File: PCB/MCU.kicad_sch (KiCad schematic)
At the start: 39 parts, among them J1 MSD-1-A, SW33V1 Conn_01x01_Pin

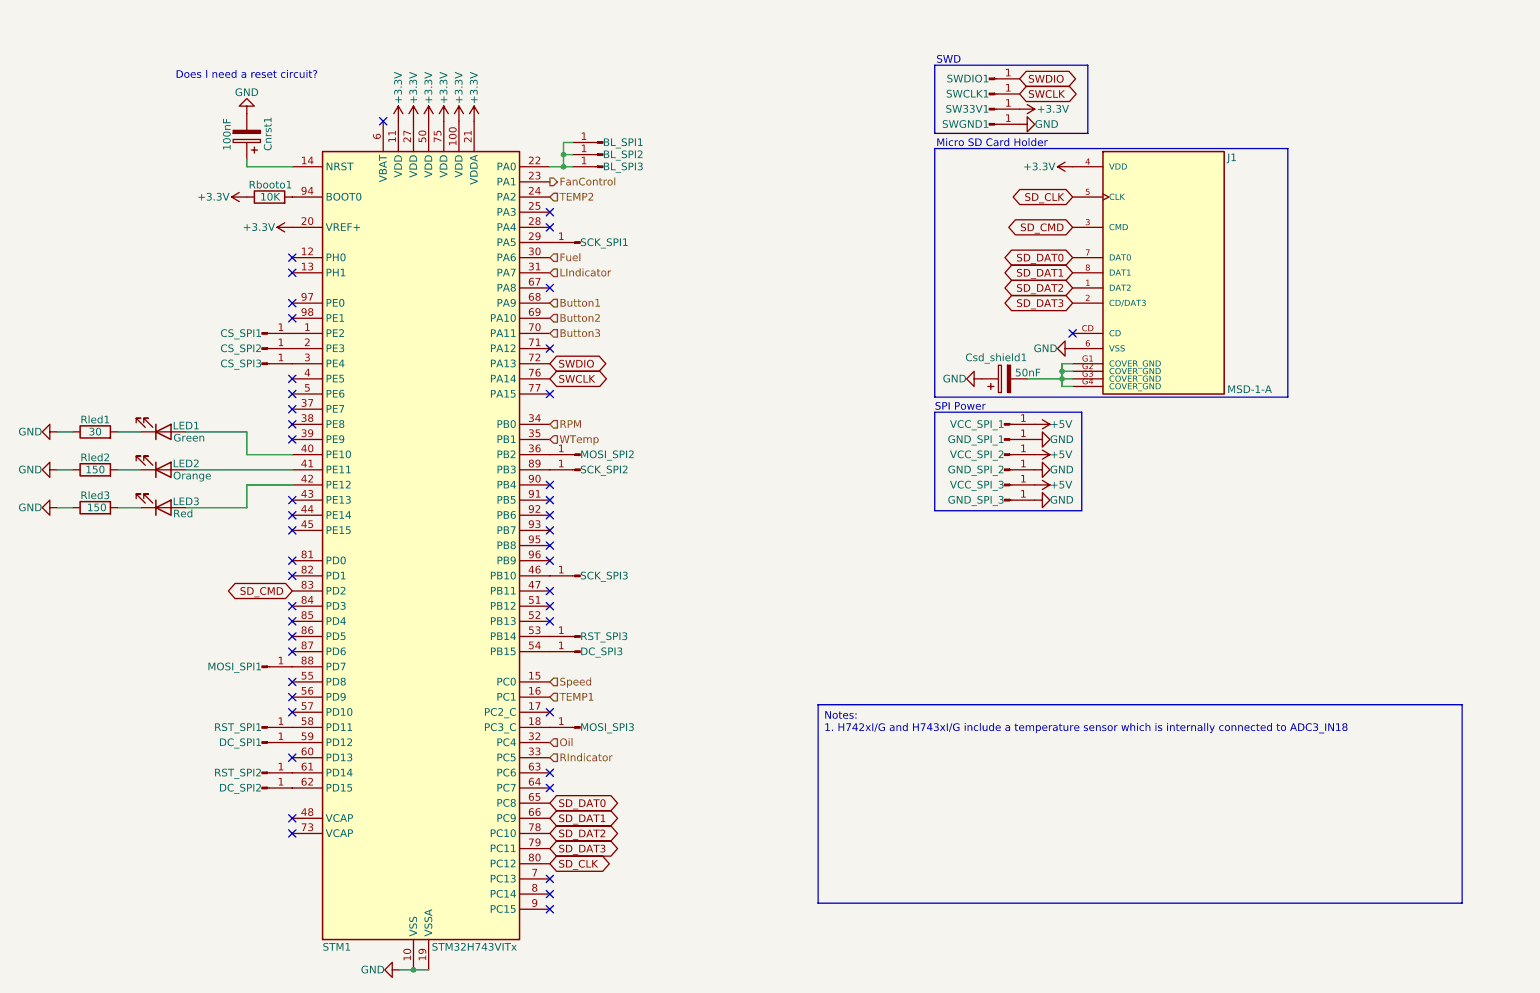
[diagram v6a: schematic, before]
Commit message: Finalized circuit design; Added PCB layout
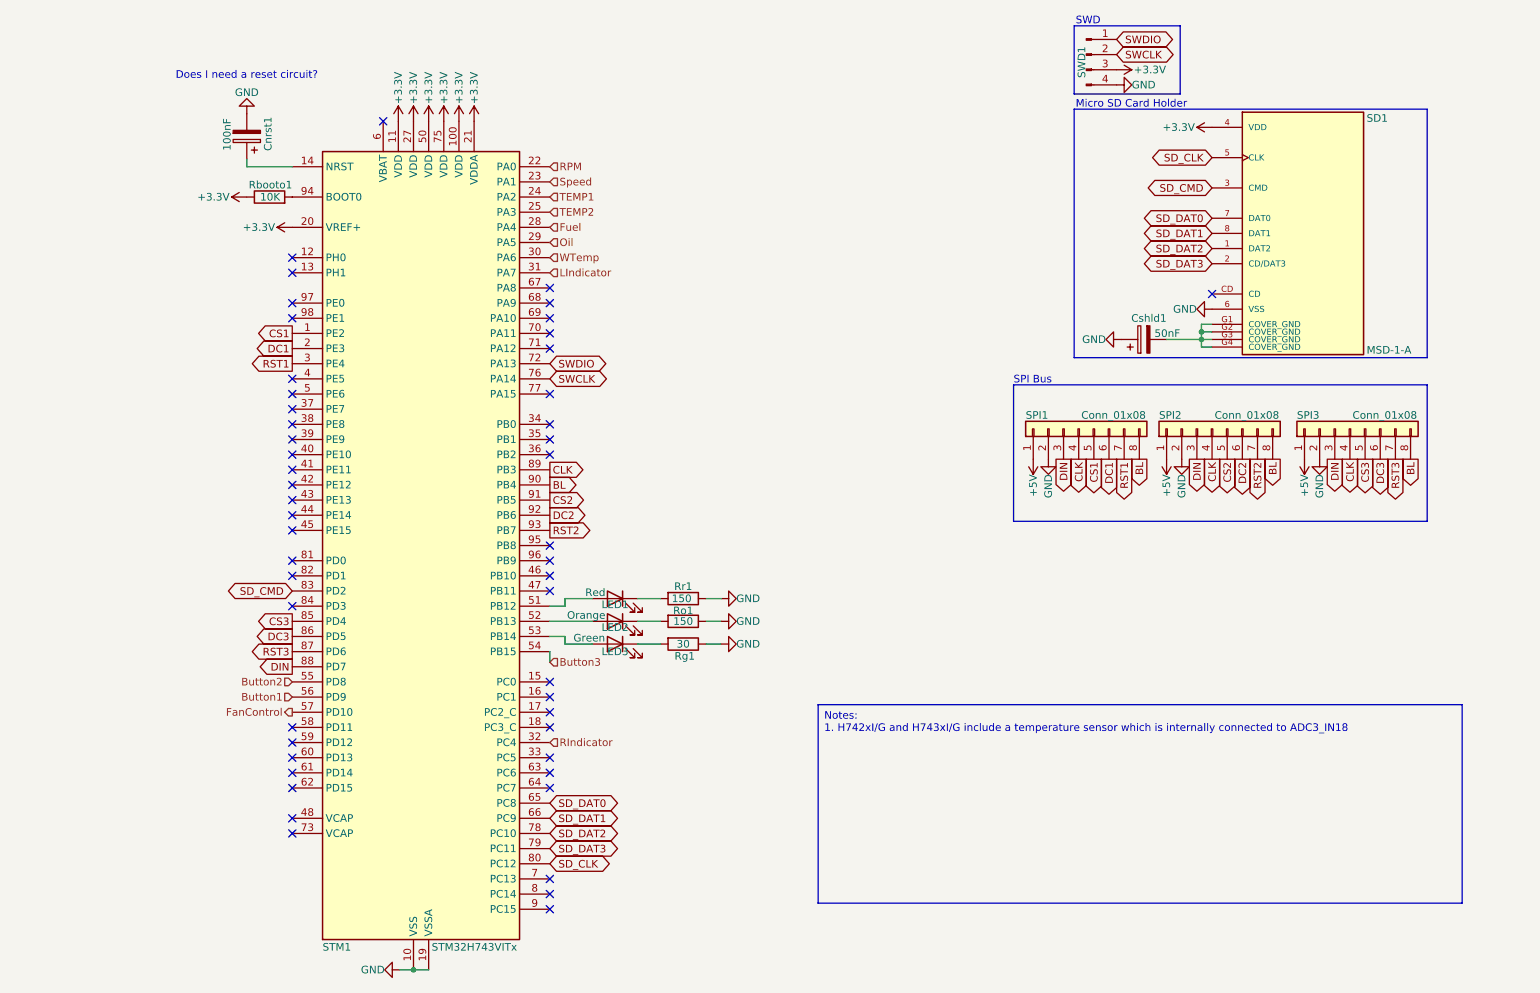
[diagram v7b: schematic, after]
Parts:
- removed BL_SPI1, BL_SPI2, BL_SPI3, CS_SPI1, CS_SPI2, CS_SPI3, DC_SPI1, DC_SPI2, DC_SPI3, GND_SPI_1, GND_SPI_2, GND_SPI_3, MOSI_SPI1, MOSI_SPI2, MOSI_SPI3, RST_SPI1, RST_SPI2, RST_SPI3, SCK_SPI1, SCK_SPI2, SCK_SPI3, SW33V1, SWCLK1, SWDIO1, SWGND1, VCC_SPI_1, VCC_SPI_2, VCC_SPI_3: Conn_01x01_Pin, Connector_PinHeader_2.54mm:PinHeader_1x01_P2.54mm_Vertical, symbol Connector:Conn_01x01_Pin
- removed Rled1: 30, Resistor_SMD:R_0603_1608Metric, symbol Device:R
- removed Rled2, Rled3: 150, Resistor_SMD:R_0603_1608Metric, symbol Device:R
- added Rg1: 30, Resistor_SMD:R_0603_1608Metric, symbol Device:R
- added Ro1, Rr1: 150, Resistor_SMD:R_0603_1608Metric, symbol Device:R
- added SPI1, SPI2, SPI3: Conn_01x08, Connector_JST:JST_SH_BM08B-SRSS-TB_1x08-1MP_P1.00mm_Vertical, symbol Connector_Generic:Conn_01x08
- added SWD1: Conn_01x04_Pin, Connector_PinHeader_2.54mm:PinHeader_1x04_P2.54mm_Vertical, symbol Connector:Conn_01x04_Pin
- LED1: value Green -> Red
- LED3: value Red -> Green
- renumbered Csd_shield1 to Cshld1, J1 to SD1
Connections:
- net +3.3V: now also SWD1.3 (Pin_3)
- net +5V: now also SPI1.1 (Pin_1), SPI2.1 (Pin_1), SPI3.1 (Pin_1)
- net Button1: now also STM1.56 (PD9); no longer STM1.68 (PA9)
- net Button2: now also STM1.55 (PD8); no longer STM1.69 (PA10)
- net Button3: now also STM1.54 (PB15); no longer STM1.70 (PA11)
- net FanControl: now also STM1.57 (PD10); no longer STM1.23 (PA1)
- net Fuel: now also STM1.28 (PA4); no longer STM1.30 (PA6)
- net GND: now also Rg1.1, Ro1.1, Rr1.1, SPI1.2 (Pin_2), SPI2.2 (Pin_2), SPI3.2 (Pin_2), SWD1.4 (Pin_4)
- net Oil: now also STM1.29 (PA5); no longer STM1.32 (PC4)
- net RIndicator: now also STM1.32 (PC4); no longer STM1.33 (PC5)
- net RPM: now also STM1.22 (PA0); no longer STM1.34 (PB0)
- net SWCLK: now also SWD1.2 (Pin_2)
- net SWDIO: now also SWD1.1 (Pin_1)
- net Speed: now also STM1.23 (PA1); no longer STM1.15 (PC0)
- net TEMP1: now also STM1.24 (PA2); no longer STM1.16 (PC1)
- net TEMP2: now also STM1.25 (PA3); no longer STM1.24 (PA2)
- net WTemp: now also STM1.30 (PA6); no longer STM1.35 (PB1)
- net DC1: now reaches STM1.2 (PE3)
- net DC1: now also SPI1.6 (Pin_6)
- net at LED2.1 (K): now also Ro1.2
- net RST1: now reaches STM1.3 (PE4)
- net RST1: now also SPI1.7 (Pin_7)
- net CS1: now reaches STM1.1 (PE2)
- net CS1: now also SPI1.5 (Pin_5)
- net at LED1.1 (K): now also Rr1.2
- net at LED1.2 (A): now also STM1.51 (PB12); no longer STM1.40 (PE10)
- net at STM1.53 (PB14): now also LED3.2 (A)
- net at LED2.2 (A): now also STM1.52 (PB13); no longer STM1.41 (PE11)
- net at STM1.42 (PE12): no longer LED3.2 (A)
- net CS3: now reaches STM1.85 (PD4)
- net CS3: now also SPI3.5 (Pin_5)
- net DC3: now reaches STM1.86 (PD5)
- net DC3: now also SPI3.6 (Pin_6)
- net RST3: now reaches STM1.87 (PD6)
- net RST3: now also SPI3.7 (Pin_7)
- net DIN: now reaches STM1.88 (PD7)
- net DIN: now also SPI1.3 (Pin_3), SPI2.3 (Pin_3), SPI3.3 (Pin_3)
- net CLK: now reaches STM1.89 (PB3)
- net CLK: now also SPI1.4 (Pin_4), SPI2.4 (Pin_4), SPI3.4 (Pin_4)
- net BL: now reaches STM1.90 (PB4)
- net BL: now also SPI1.8 (Pin_8), SPI2.8 (Pin_8), SPI3.8 (Pin_8)
- net CS2: now reaches STM1.91 (PB5)
- net CS2: now also SPI2.5 (Pin_5)
- net DC2: now reaches STM1.92 (PB6)
- net DC2: now also SPI2.6 (Pin_6)
- net RST2: now reaches STM1.93 (PB7)
- net RST2: now also SPI2.7 (Pin_7)
- net at LED3.1 (K): now also Rg1.2
- no-connect marks 46 -> 50
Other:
- note added: "SPI Bus"
- note removed: "SPI Power"
- moved on the sheet: Cshld1, SD1
